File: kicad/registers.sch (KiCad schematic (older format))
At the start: 0 parts

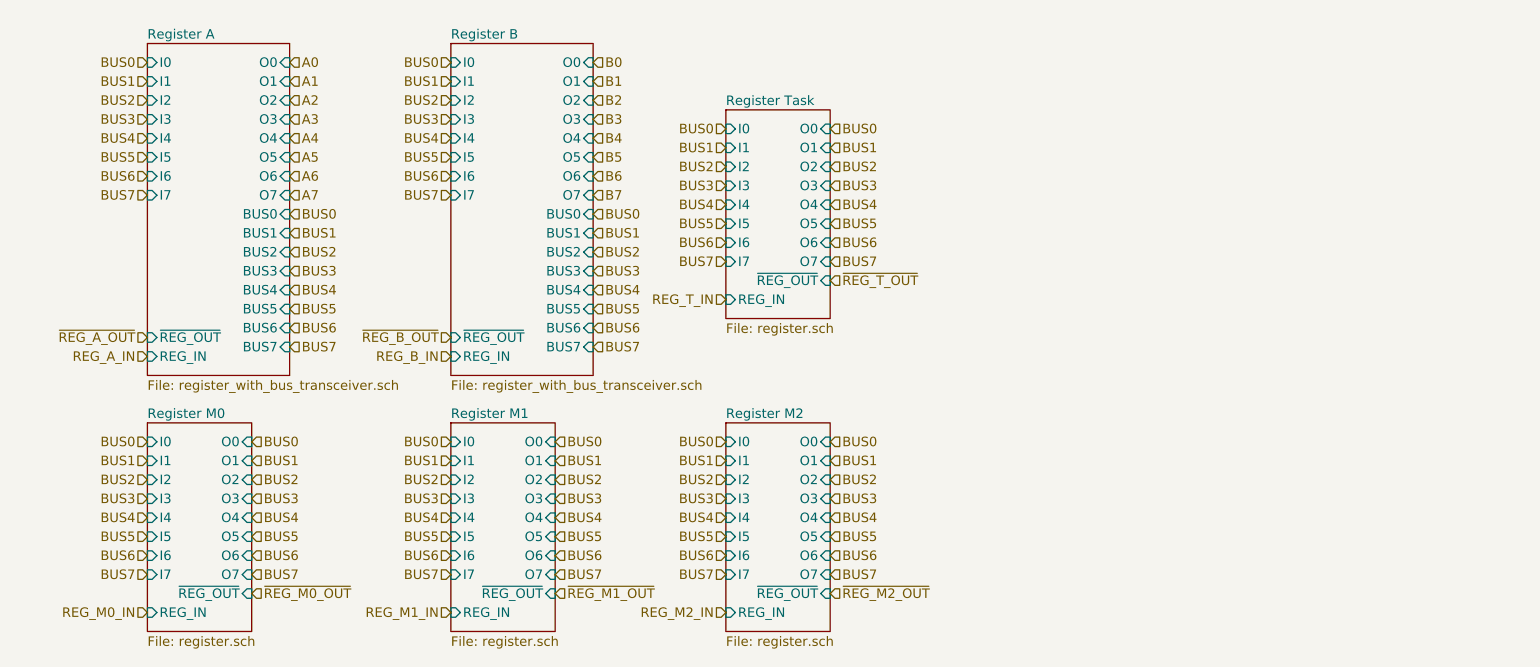
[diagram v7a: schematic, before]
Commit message: Finish MMU schematic.
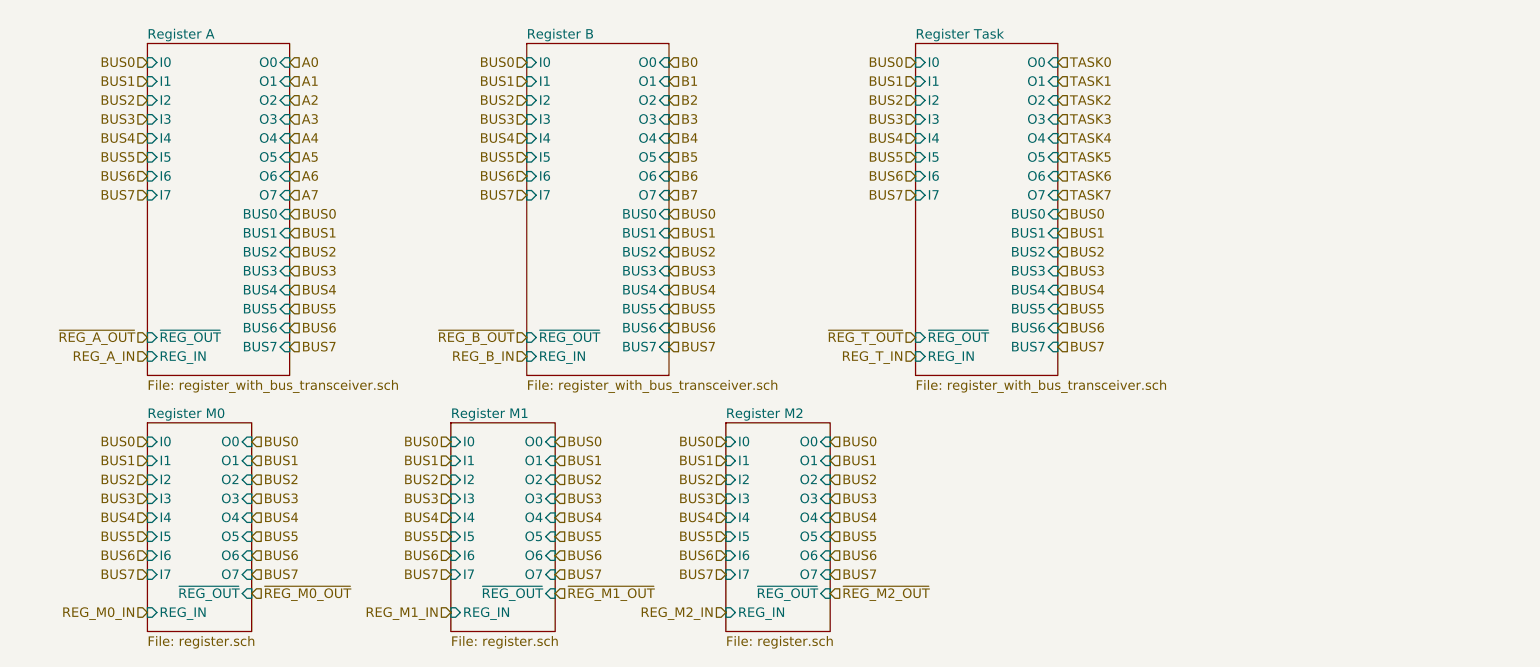
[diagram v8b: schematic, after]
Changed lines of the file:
@@
 Text HLabel 1000 2350 0    50   Input ~ 0
 ~REG_A_OUT
-Text HLabel 2600 2450 0    50   Input ~ 0
+Text HLabel 3000 2450 0    50   Input ~ 0
 REG_B_IN
-Text HLabel 2600 2350 0    50   Input ~ 0
+Text HLabel 3000 2350 0    50   Input ~ 0
 ~REG_B_OUT
 $Sheet
@@
 Text HLabel 4600 3700 2    50   Input ~ 0
 ~REG_M2_OUT
-$Sheet
-S 4050 1150 550  1100
-U 5AFD86BE
-F0 "Register Task" 50
-F1 "register.sch" 50
-F2 "REG_IN" I L 4050 2150 50
-F3 "I0" I L 4050 1250 50
-F4 "I1" I L 4050 1350 50
-F5 "I2" I L 4050 1450 50
-F6 "I3" I L 4050 1550 50
-F7 "I4" I L 4050 1650 50
-F8 "I5" I L 4050 1750 50
-F9 "I6" I L 4050 1850 50
-F10 "I7" I L 4050 1950 50
-F11 "~REG_OUT" I R 4600 2050 50
-F12 "O0" I R 4600 1250 50
-F13 "O1" I R 4600 1350 50
-F14 "O2" I R 4600 1450 50
-F15 "O3" I R 4600 1550 50
-F16 "O4" I R 4600 1650 50
-F17 "O5" I R 4600 1750 50
-F18 "O6" I R 4600 1850 50
-F19 "O7" I R 4600 1950 50
-$EndSheet
-Text HLabel 4050 1250 0    50   Input ~ 0
-BUS0
-Text HLabel 4050 1350 0    50   Input ~ 0
-BUS1
-Text HLabel 4050 1450 0    50   Input ~ 0
-BUS2
-Text HLabel 4050 1550 0    50   Input ~ 0
-BUS3
-Text HLabel 4050 1650 0    50   Input ~ 0
-BUS4
-Text HLabel 4050 1750 0    50   Input ~ 0
-BUS5
-Text HLabel 4050 1850 0    50   Input ~ 0
-BUS6
-Text HLabel 4050 1950 0    50   Input ~ 0
-BUS7
-Text HLabel 4600 1250 2    50   Input ~ 0
-BUS0
-Text HLabel 4600 1350 2    50   Input ~ 0
-BUS1
-Text HLabel 4600 1450 2    50   Input ~ 0
-BUS2
-Text HLabel 4600 1550 2    50   Input ~ 0
-BUS3
-Text HLabel 4600 1650 2    50   Input ~ 0
-BUS4
-Text HLabel 4600 1750 2    50   Input ~ 0
-BUS5
-Text HLabel 4600 1850 2    50   Input ~ 0
-BUS6
-Text HLabel 4600 1950 2    50   Input ~ 0
-BUS7
-Text HLabel 4050 2150 0    50   Input ~ 0
+Text HLabel 5800 1700 2    50   Input ~ 0
+BUS0
+Text HLabel 5800 1800 2    50   Input ~ 0
+BUS1
+Text HLabel 5800 1900 2    50   Input ~ 0
+BUS2
+Text HLabel 5800 2000 2    50   Input ~ 0
+BUS3
+Text HLabel 5800 2100 2    50   Input ~ 0
+BUS4
+Text HLabel 5800 2200 2    50   Input ~ 0
+BUS5
+Text HLabel 5800 2300 2    50   Input ~ 0
+BUS6
+Text HLabel 5800 2400 2    50   Input ~ 0
+BUS7
+Text HLabel 5050 2450 0    50   Input ~ 0
 REG_T_IN
-Text HLabel 4600 2050 2    50   Input ~ 0
+Text HLabel 5050 2350 0    50   Input ~ 0
 ~REG_T_OUT
 $Sheet
@@
 F27 "BUS7" I R 1750 2400 50
 $EndSheet
-Text HLabel 2600 900  0    50   Input ~ 0
-BUS0
-Text HLabel 2600 1000 0    50   Input ~ 0
-BUS1
-Text HLabel 2600 1100 0    50   Input ~ 0
-BUS2
-Text HLabel 2600 1200 0    50   Input ~ 0
-BUS3
-Text HLabel 2600 1300 0    50   Input ~ 0
-BUS4
-Text HLabel 2600 1400 0    50   Input ~ 0
-BUS5
-Text HLabel 2600 1500 0    50   Input ~ 0
-BUS6
-Text HLabel 2600 1600 0    50   Input ~ 0
-BUS7
-Text HLabel 3350 1700 2    50   Input ~ 0
-BUS0
-Text HLabel 3350 1800 2    50   Input ~ 0
-BUS1
-Text HLabel 3350 1900 2    50   Input ~ 0
-BUS2
-Text HLabel 3350 2000 2    50   Input ~ 0
-BUS3
-Text HLabel 3350 2100 2    50   Input ~ 0
-BUS4
-Text HLabel 3350 2200 2    50   Input ~ 0
-BUS5
-Text HLabel 3350 2300 2    50   Input ~ 0
-BUS6
-Text HLabel 3350 2400 2    50   Input ~ 0
-BUS7
-$Sheet
-S 2600 800  750  1750
-U 5AFD336A
-F0 "Register B" 50
-F1 "register_with_bus_transceiver.sch" 50
-F2 "REG_IN" I L 2600 2450 50
-F3 "I0" I L 2600 900 50
-F4 "I1" I L 2600 1000 50
-F5 "I2" I L 2600 1100 50
-F6 "I3" I L 2600 1200 50
-F7 "I4" I L 2600 1300 50
-F8 "I5" I L 2600 1400 50
-F9 "I6" I L 2600 1500 50
-F10 "I7" I L 2600 1600 50
-F11 "~REG_OUT" I L 2600 2350 50
-F12 "O0" I R 3350 900 50
-F13 "O1" I R 3350 1000 50
-F14 "O2" I R 3350 1100 50
-F15 "O3" I R 3350 1200 50
-F16 "O4" I R 3350 1300 50
-F17 "O5" I R 3350 1400 50
-F18 "O6" I R 3350 1500 50
-F19 "O7" I R 3350 1600 50
-F20 "BUS0" I R 3350 1700 50
-F21 "BUS1" I R 3350 1800 50
-F22 "BUS2" I R 3350 1900 50
-F23 "BUS3" I R 3350 2000 50
-F24 "BUS4" I R 3350 2100 50
-F25 "BUS5" I R 3350 2200 50
-F26 "BUS6" I R 3350 2300 50
-F27 "BUS7" I R 3350 2400 50
-$EndSheet
+Text HLabel 3000 900  0    50   Input ~ 0
+BUS0
+Text HLabel 3000 1000 0    50   Input ~ 0
+BUS1
+Text HLabel 3000 1100 0    50   Input ~ 0
+BUS2
+Text HLabel 3000 1200 0    50   Input ~ 0
+BUS3
+Text HLabel 3000 1300 0    50   Input ~ 0
+BUS4
+Text HLabel 3000 1400 0    50   Input ~ 0
+BUS5
+Text HLabel 3000 1500 0    50   Input ~ 0
+BUS6
+Text HLabel 3000 1600 0    50   Input ~ 0
+BUS7
+Text HLabel 3750 1700 2    50   Input ~ 0
+BUS0
+Text HLabel 3750 1800 2    50   Input ~ 0
+BUS1
+Text HLabel 3750 1900 2    50   Input ~ 0
+BUS2
+Text HLabel 3750 2000 2    50   Input ~ 0
+BUS3
+Text HLabel 3750 2100 2    50   Input ~ 0
+BUS4
+Text HLabel 3750 2200 2    50   Input ~ 0
+BUS5
+Text HLabel 3750 2300 2    50   Input ~ 0
+BUS6
+Text HLabel 3750 2400 2    50   Input ~ 0
+BUS7
 Text HLabel 1750 900  2    50   Input ~ 0
 A0
@@
 Text HLabel 1750 1600 2    50   Input ~ 0
 A7
-Text HLabel 3350 900  2    50   Input ~ 0
+Text HLabel 3750 900  2    50   Input ~ 0
 B0
-Text HLabel 3350 1000 2    50   Input ~ 0
+Text HLabel 3750 1000 2    50   Input ~ 0
 B1
-Text HLabel 3350 1100 2    50   Input ~ 0
+Text HLabel 3750 1100 2    50   Input ~ 0
 B2
-Text HLabel 3350 1200 2    50   Input ~ 0
+Text HLabel 3750 1200 2    50   Input ~ 0
 B3
-Text HLabel 3350 1300 2    50   Input ~ 0
+Text HLabel 3750 1300 2    50   Input ~ 0
 B4
-Text HLabel 3350 1400 2    50   Input ~ 0
+Text HLabel 3750 1400 2    50   Input ~ 0
 B5
-Text HLabel 3350 1500 2    50   Input ~ 0
+Text HLabel 3750 1500 2    50   Input ~ 0
 B6
-Text HLabel 3350 1600 2    50   Input ~ 0
+Text HLabel 3750 1600 2    50   Input ~ 0
 B7
+$Sheet
+S 3000 800  750  1750
+U 5B0AB8A7
+F0 "Register B" 50
+F1 "register_with_bus_transceiver.sch" 50
+F2 "REG_IN" I L 3000 2450 50
+F3 "I0" I L 3000 900 50
+F4 "I1" I L 3000 1000 50
+F5 "I2" I L 3000 1100 50
+F6 "I3" I L 3000 1200 50
+F7 "I4" I L 3000 1300 50
+F8 "I5" I L 3000 1400 50
+F9 "I6" I L 3000 1500 50
+F10 "I7" I L 3000 1600 50
+F11 "~REG_OUT" I L 3000 2350 50
+F12 "O0" I R 3750 900 50
+F13 "O1" I R 3750 1000 50
+F14 "O2" I R 3750 1100 50
+F15 "O3" I R 3750 1200 50
+F16 "O4" I R 3750 1300 50
+F17 "O5" I R 3750 1400 50
+F18 "O6" I R 3750 1500 50
+F19 "O7" I R 3750 1600 50
+F20 "BUS0" I R 3750 1700 50
+F21 "BUS1" I R 3750 1800 50
+F22 "BUS2" I R 3750 1900 50
+F23 "BUS3" I R 3750 2000 50
+F24 "BUS4" I R 3750 2100 50
+F25 "BUS5" I R 3750 2200 50
+F26 "BUS6" I R 3750 2300 50
+F27 "BUS7" I R 3750 2400 50
+$EndSheet
+$Sheet
+S 5050 800  750  1750
+U 5AFD336A
+F0 "Register Task" 50
+F1 "register_with_bus_transceiver.sch" 50
+F2 "REG_IN" I L 5050 2450 50
+F3 "I0" I L 5050 900 50
+F4 "I1" I L 5050 1000 50
+F5 "I2" I L 5050 1100 50
+F6 "I3" I L 5050 1200 50
+F7 "I4" I L 5050 1300 50
+F8 "I5" I L 5050 1400 50
+F9 "I6" I L 5050 1500 50
+F10 "I7" I L 5050 1600 50
+F11 "~REG_OUT" I L 5050 2350 50
+F12 "O0" I R 5800 900 50
+F13 "O1" I R 5800 1000 50
+F14 "O2" I R 5800 1100 50
+F15 "O3" I R 5800 1200 50
+F16 "O4" I R 5800 1300 50
+F17 "O5" I R 5800 1400 50
+F18 "O6" I R 5800 1500 50
+F19 "O7" I R 5800 1600 50
+F20 "BUS0" I R 5800 1700 50
+F21 "BUS1" I R 5800 1800 50
+F22 "BUS2" I R 5800 1900 50
+F23 "BUS3" I R 5800 2000 50
+F24 "BUS4" I R 5800 2100 50
+F25 "BUS5" I R 5800 2200 50
+F26 "BUS6" I R 5800 2300 50
+F27 "BUS7" I R 5800 2400 50
+$EndSheet
+Text HLabel 5050 900  0    50   Input ~ 0
+BUS0
+Text HLabel 5050 1000 0    50   Input ~ 0
+BUS1
+Text HLabel 5050 1100 0    50   Input ~ 0
+BUS2
+Text HLabel 5050 1200 0    50   Input ~ 0
+BUS3
+Text HLabel 5050 1300 0    50   Input ~ 0
+BUS4
+Text HLabel 5050 1400 0    50   Input ~ 0
+BUS5
+Text HLabel 5050 1500 0    50   Input ~ 0
+BUS6
+Text HLabel 5050 1600 0    50   Input ~ 0
+BUS7
+Text HLabel 5800 900  2    50   Input ~ 0
+TASK0
+Text HLabel 5800 1000 2    50   Input ~ 0
+TASK1
+Text HLabel 5800 1100 2    50   Input ~ 0
+TASK2
+Text HLabel 5800 1200 2    50   Input ~ 0
+TASK3
+Text HLabel 5800 1300 2    50   Input ~ 0
+TASK4
+Text HLabel 5800 1400 2    50   Input ~ 0
+TASK5
+Text HLabel 5800 1500 2    50   Input ~ 0
+TASK6
+Text HLabel 5800 1600 2    50   Input ~ 0
+TASK7
 $EndSCHEMATC
